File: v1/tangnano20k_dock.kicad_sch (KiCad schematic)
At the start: 50 parts, among them J1 Mini-DIN-6, J2 Conn_01x02, J3 DB15_Female_HighDensity, J4 DB9_Male, J5 Conn_02x16_Odd_Even, J6 FCR684205T, J7 RCA, J8 RCA, J9 RCA, U1 TXS0104E, U2 TangNano20K, U3 CS4354

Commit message: Everything connected
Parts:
- removed J3: DB15_Female_HighDensity, Connector_Dsub:DSUB-15-HD_Female_Horizontal_P2.29x1.98mm_EdgePinOffset9.40mm, symbol Connector:DB15_Female_HighDensity
- removed J5: Conn_02x16_Odd_Even, Connector_PinHeader_2.54mm:PinHeader_2x16_P2.54mm_Vertical, symbol Connector_Generic:Conn_02x16_Odd_Even
- removed J8, J9: RCA, TangNano20k:phono, symbol Connector:Conn_Coaxial
- added J3: DB15_Female_HighDensity_MountingHoles, Connector_Dsub:DSUB-15-HD_Female_Horizontal_P2.29x1.98mm_EdgePinOffset8.35mm_Housed_MountingHolesOffset10.89mm, symbol Connector:DB15_Female_HighDensity_MountingHoles
- added J5, J6: Conn_02x10_Odd_Even, Connector_PinHeader_2.54mm:PinHeader_2x10_P2.54mm_Vertical, symbol Connector_Generic:Conn_02x10_Odd_Even
- added J9: AudioJack3, Connector_Audio:Jack_3.5mm_Lumberg_1503_07_Horizontal, symbol Connector:AudioJack3
- renumbered J6 to J8
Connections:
- net GND: now also J3.0, J3.10, J3.5, J3.6, J3.7, J3.8, J5.1 (Pin_1), J5.2 (Pin_2), J6.1 (Pin_1), J6.2 (Pin_2), J9.S
- net GPIO0: now also J6.3 (Pin_3)
- net GPIO1: now also J6.5 (Pin_5)
- net GPIO10: now also J5.7 (Pin_7)
- net GPIO11: now also J5.9 (Pin_9)
- net GPIO12: now also J5.11 (Pin_11)
- net GPIO13: now also J5.13 (Pin_13)
- net GPIO14: now also J5.15 (Pin_15)
- net GPIO15: now also J5.17 (Pin_17)
- net GPIO2: now also J6.7 (Pin_7)
- net GPIO3: now also J6.9 (Pin_9)
- net GPIO4: now also J6.11 (Pin_11)
- net GPIO5: now also J6.13 (Pin_13)
- net GPIO6: now also J6.15 (Pin_15)
- net GPIO7: now also J6.17 (Pin_17)
- net GPIO8: now also J5.3 (Pin_3)
- net GPIO9: now also J5.5 (Pin_5)
- net VGA_B: now also J3.3
- net VGA_G: now also J3.2
- net VGA_HS: now also J3.13
- net VGA_R: now also J3.1
- net VGA_VS: now also J3.14
- net at RN1.2 (R1): now also J5.4 (Pin_4)
- net at RN1.3 (R2): now also J5.6 (Pin_6)
- net at RN1.4 (R3): now also J5.8 (Pin_8)
- net at RN1.5 (R4): now also J5.10 (Pin_10)
- net at RN1.6 (R5): now also J5.12 (Pin_12)
- net at RN1.7 (R6): now also J5.14 (Pin_14)
- net at RN1.8 (R7): now also J5.16 (Pin_16)
- net at RN1.9 (R8): now also J5.18 (Pin_18)
- net at C10.2, JP2.2 (C): now also J9.T
- net at C11.2, JP3.2 (C): now also J9.R
- net at RN2.2 (R1): now also J6.4 (Pin_4)
- net at RN2.3 (R2): now also J6.6 (Pin_6)
- net at RN2.4 (R3): now also J6.8 (Pin_8)
- net at RN2.5 (R4): now also J6.10 (Pin_10)
- net at RN2.6 (R5): now also J6.12 (Pin_12)
- net at RN2.7 (R6): now also J6.14 (Pin_14)
- net at RN2.8 (R7): now also J6.16 (Pin_16)
- net at RN2.9 (R8): now also J6.18 (Pin_18)
- no-connect marks 8 -> 12
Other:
- note removed: "Left"
- note removed: "Right"
- moved on the sheet: RN1, RN2

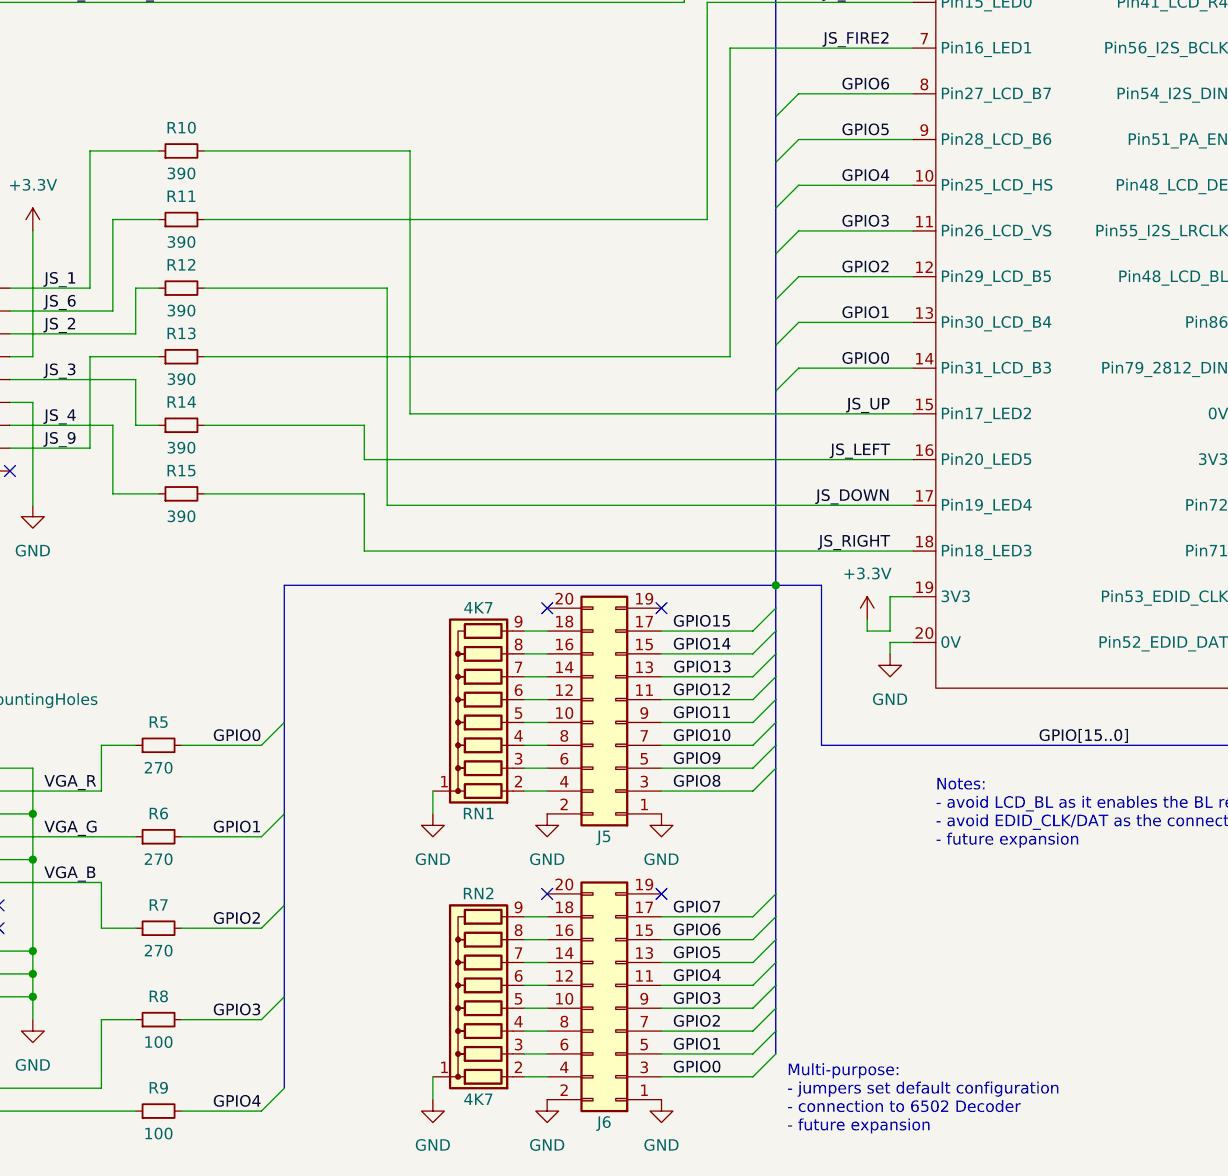
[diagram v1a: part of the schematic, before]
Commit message: Much tidying up, corrected VGA footprint
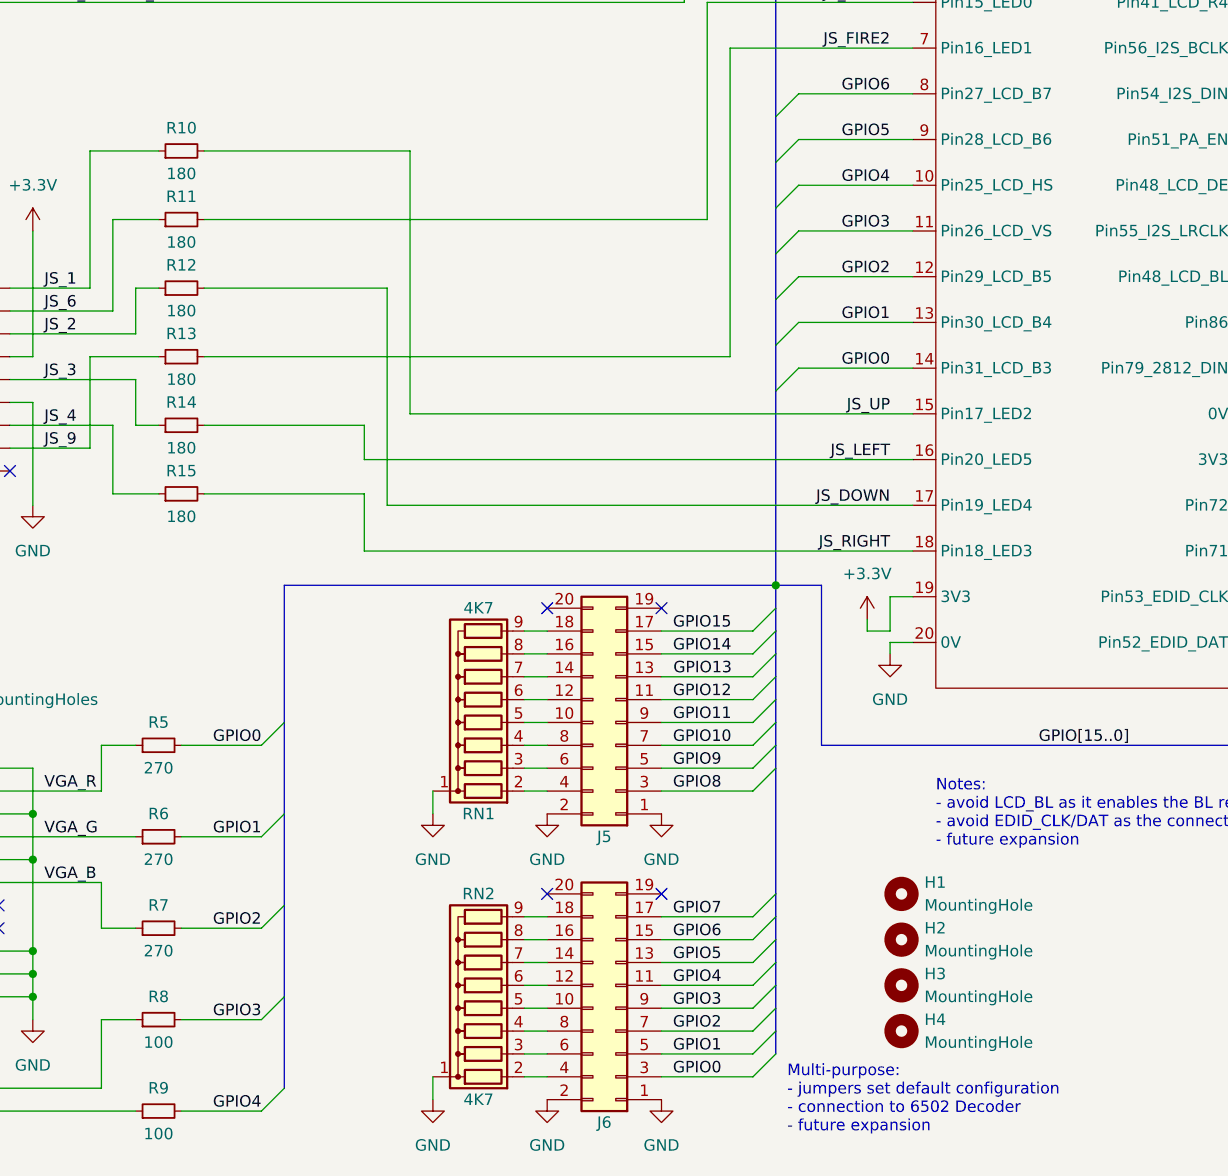
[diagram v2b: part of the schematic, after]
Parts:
- added H1, H2, H3, H4: MountingHole, MountingHole:MountingHole_3.2mm_M3, symbol Mechanical:MountingHole
- J3: footprint Connector_Dsub:DSUB-15-HD_Female_Horizontal_P2.29x1.98mm_EdgePinOffset8.35mm_Housed_MountingHolesOffset10.89mm -> TangNano20k:DSUB-15-HD_Female_Horizontal_P2.29x1.98mm_EdgePinOffset8.35mm_Housed_MountingHolesOffset10.89mm
- J9: footprint Connector_Audio:Jack_3.5mm_Lumberg_1503_07_Horizontal -> TangNano20k:Jack_3.5mm_Lumberg_1503_07_Horizontal
- R10, R11, R12, R13, R14, R15: value 390 -> 180
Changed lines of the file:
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@@
     (property "Reference" "J3" (id 0) (at 33.02 143.51 0))
     (property "Value" "DB15_Female_HighDensity_MountingHoles" (id 1) (at 33.02 146.05 0))
-    (property "Footprint" "Connector_Dsub:DSUB-15-HD_Female_Horizontal_P2.29x1.98mm_EdgePinOffset8.35mm_Housed_MountingHolesOffset10.89mm" (id 2) (at 57.15 156.21 0)
+    (property "Footprint" "TangNano20k:DSUB-15-HD_Female_Horizontal_P2.29x1.98mm_EdgePinOffset8.35mm_Housed_MountingHolesOffset10.89mm" (id 2) (at 57.15 156.21 0)
       (effects (font (size 1.27 1.27)) hide)
     )
@@
     (pin "1")
   )
+  (symbol (lib_id "Mechanical:MountingHole") (at 140.97 182.88 0) (unit 1)
+    (in_bom yes) (on_board yes) (fields_autoplaced)
+    (property "Reference" "H4" (id 0) (at 143.51 181.6099 0)
+      (effects (font (size 1.27 1.27)) (justify left))
+    )
+    (property "Value" "MountingHole" (id 1) (at 143.51 184.1499 0)
+      (effects (font (size 1.27 1.27)) (justify left))
+    )
+    (property "Footprint" "MountingHole:MountingHole_3.2mm_M3" (id 2) (at 140.97 182.88 0)
+      (effects (font (size 1.27 1.27)) hide)
+    )
+    (property "Datasheet" "~" (id 3) (at 140.97 182.88 0)
+      (effects (font (size 1.27 1.27)) hide)
+    )
+  )
   (symbol (lib_id "Device:C_Small") (at 210.82 24.13 0) (mirror x) (unit 1)
     (in_bom yes) (on_board yes) (fields_autoplaced)
@@
     (pin "1")
   )
+  (symbol (lib_id "Mechanical:MountingHole") (at 140.97 167.64 0) (unit 1)
+    (in_bom yes) (on_board yes) (fields_autoplaced)
+    (property "Reference" "H1" (id 0) (at 143.51 166.3699 0)
+      (effects (font (size 1.27 1.27)) (justify left))
+    )
+    (property "Value" "MountingHole" (id 1) (at 143.51 168.9099 0)
+      (effects (font (size 1.27 1.27)) (justify left))
+    )
+    (property "Footprint" "MountingHole:MountingHole_3.2mm_M3" (id 2) (at 140.97 167.64 0)
+      (effects (font (size 1.27 1.27)) hide)
+    )
+    (property "Datasheet" "~" (id 3) (at 140.97 167.64 0)
+      (effects (font (size 1.27 1.27)) hide)
+    )
+  )
   (symbol (lib_id "Device:R_Small") (at 60.96 123.19 90) (unit 1)
     (in_bom yes) (on_board yes)
     (property "Reference" "R15" (id 0) (at 60.96 120.65 90))
-    (property "Value" "390" (id 1) (at 60.96 125.73 90))
+    (property "Value" "180" (id 1) (at 60.96 125.73 90))
     (property "Footprint" "Resistor_THT:R_Axial_DIN0207_L6.3mm_D2.5mm_P10.16mm_Horizontal" (id 2) (at 60.96 123.19 0)
       (effects (font (size 1.27 1.27)) hide)
@@
       (effects (font (size 1.27 1.27)) (justify right))
     )
-    (property "Footprint" "Connector_Audio:Jack_3.5mm_Lumberg_1503_07_Horizontal" (id 2) (at 278.13 109.22 0)
+    (property "Footprint" "TangNano20k:Jack_3.5mm_Lumberg_1503_07_Horizontal" (id 2) (at 278.13 109.22 0)
       (effects (font (size 1.27 1.27)) hide)
     )
@@
     (in_bom yes) (on_board yes)
     (property "Reference" "R11" (id 0) (at 60.96 90.17 90))
-    (property "Value" "390" (id 1) (at 60.96 95.25 90))
+    (property "Value" "180" (id 1) (at 60.96 95.25 90))
     (property "Footprint" "Resistor_THT:R_Axial_DIN0207_L6.3mm_D2.5mm_P10.16mm_Horizontal" (id 2) (at 60.96 92.71 0)
       (effects (font (size 1.27 1.27)) hide)
@@
     (in_bom yes) (on_board yes)
     (property "Reference" "R12" (id 0) (at 60.96 97.79 90))
-    (property "Value" "390" (id 1) (at 60.96 102.87 90))
+    (property "Value" "180" (id 1) (at 60.96 102.87 90))
     (property "Footprint" "Resistor_THT:R_Axial_DIN0207_L6.3mm_D2.5mm_P10.16mm_Horizontal" (id 2) (at 60.96 100.33 0)
       (effects (font (size 1.27 1.27)) hide)
@@
     (pin "8")
     (pin "9")
+  )
+  (symbol (lib_id "Mechanical:MountingHole") (at 140.97 177.8 0) (unit 1)
+    (in_bom yes) (on_board yes) (fields_autoplaced)
+    (property "Reference" "H3" (id 0) (at 143.51 176.5299 0)
+      (effects (font (size 1.27 1.27)) (justify left))
+    )
+    (property "Value" "MountingHole" (id 1) (at 143.51 179.0699 0)
+      (effects (font (size 1.27 1.27)) (justify left))
+    )
+    (property "Footprint" "MountingHole:MountingHole_3.2mm_M3" (id 2) (at 140.97 177.8 0)
+      (effects (font (size 1.27 1.27)) hide)
+    )
+    (property "Datasheet" "~" (id 3) (at 140.97 177.8 0)
+      (effects (font (size 1.27 1.27)) hide)
+    )
   )
   (symbol (lib_id "Device:R_Small") (at 58.42 151.13 90) (unit 1)
@@
     (in_bom yes) (on_board yes)
     (property "Reference" "R13" (id 0) (at 60.96 105.41 90))
-    (property "Value" "390" (id 1) (at 60.96 110.49 90))
+    (property "Value" "180" (id 1) (at 60.96 110.49 90))
     (property "Footprint" "Resistor_THT:R_Axial_DIN0207_L6.3mm_D2.5mm_P10.16mm_Horizontal" (id 2) (at 60.96 107.95 0)
       (effects (font (size 1.27 1.27)) hide)
@@
     (in_bom yes) (on_board yes)
     (property "Reference" "R14" (id 0) (at 60.96 113.03 90))
-    (property "Value" "390" (id 1) (at 60.96 118.11 90))
+    (property "Value" "180" (id 1) (at 60.96 118.11 90))
     (property "Footprint" "Resistor_THT:R_Axial_DIN0207_L6.3mm_D2.5mm_P10.16mm_Horizontal" (id 2) (at 60.96 115.57 0)
       (effects (font (size 1.27 1.27)) hide)
@@
     (in_bom yes) (on_board yes)
     (property "Reference" "R10" (id 0) (at 60.96 82.55 90))
-    (property "Value" "390" (id 1) (at 60.96 87.63 90))
+    (property "Value" "180" (id 1) (at 60.96 87.63 90))
     (property "Footprint" "Resistor_THT:R_Axial_DIN0207_L6.3mm_D2.5mm_P10.16mm_Horizontal" (id 2) (at 60.96 85.09 0)
       (effects (font (size 1.27 1.27)) hide)
@@
     (pin "1")
   )
+  (symbol (lib_id "Mechanical:MountingHole") (at 140.97 172.72 0) (unit 1)
+    (in_bom yes) (on_board yes) (fields_autoplaced)
+    (property "Reference" "H2" (id 0) (at 143.51 171.4499 0)
+      (effects (font (size 1.27 1.27)) (justify left))
+    )
+    (property "Value" "MountingHole" (id 1) (at 143.51 173.9899 0)
+      (effects (font (size 1.27 1.27)) (justify left))
+    )
+    (property "Footprint" "MountingHole:MountingHole_3.2mm_M3" (id 2) (at 140.97 172.72 0)
+      (effects (font (size 1.27 1.27)) hide)
+    )
+    (property "Datasheet" "~" (id 3) (at 140.97 172.72 0)
+      (effects (font (size 1.27 1.27)) hide)
+    )
+  )
   (symbol (lib_id "power:GND") (at 245.11 38.1 0) (unit 1)
     (in_bom yes) (on_board yes) (fields_autoplaced)
@@
       (reference "C11") (unit 1) (value "2n2") (footprint "Capacitor_THT:C_Disc_D5.0mm_W2.5mm_P2.50mm")
     )
+    (path "/3efa4c66-1bea-40a4-bda9-02b28c07af29"
+      (reference "H1") (unit 1) (value "MountingHole") (footprint "MountingHole:MountingHole_3.2mm_M3")
+    )
+    (path "/f95e5f0b-56a0-442b-9f1b-cce491951b72"
+      (reference "H2") (unit 1) (value "MountingHole") (footprint "MountingHole:MountingHole_3.2mm_M3")
+    )
+    (path "/820967dd-e818-4da1-bb9b-2a6bbdeea89d"
+      (reference "H3") (unit 1) (value "MountingHole") (footprint "MountingHole:MountingHole_3.2mm_M3")
+    )
+    (path "/2edda0e4-403b-45ec-b8d6-bae5fe9a549d"
+      (reference "H4") (unit 1) (value "MountingHole") (footprint "MountingHole:MountingHole_3.2mm_M3")
+    )
     (path "/9becf180-126c-4cc1-ba0f-3c658ab540d4"
       (reference "J1") (unit 1) (value "Mini-DIN-6") (footprint "TangNano20k:minidin6")
@@
     )
     (path "/06f8946b-c0d3-4d8e-bc44-a3a97fa77958"
-      (reference "J3") (unit 1) (value "DB15_Female_HighDensity_MountingHoles") (footprint "Connector_Dsub:DSUB-15-HD_Female_Horizontal_P2.29x1.98mm_EdgePinOffset8.35mm_Housed_MountingHolesOffset10.89mm")
+      (reference "J3") (unit 1) (value "DB15_Female_HighDensity_MountingHoles") (footprint "TangNano20k:DSUB-15-HD_Female_Horizontal_P2.29x1.98mm_EdgePinOffset8.35mm_Housed_MountingHolesOffset10.89mm")
     )
     (path "/8d13ec8a-0e85-4cb6-815a-22cecb20a93c"
@@
     )
     (path "/4877468b-ee74-43f7-a4dc-6a0ddb9f2b4d"
-      (reference "J9") (unit 1) (value "AudioJack3") (footprint "Connector_Audio:Jack_3.5mm_Lumberg_1503_07_Horizontal")
+      (reference "J9") (unit 1) (value "AudioJack3") (footprint "TangNano20k:Jack_3.5mm_Lumberg_1503_07_Horizontal")
     )
     (path "/af9d2222-45eb-4253-a2c0-2a0bf1e346a6"
@@
     )
     (path "/ec860be2-adfe-4b02-922f-502025aff678"
-      (reference "R10") (unit 1) (value "390") (footprint "Resistor_THT:R_Axial_DIN0207_L6.3mm_D2.5mm_P10.16mm_Horizontal")
+      (reference "R10") (unit 1) (value "180") (footprint "Resistor_THT:R_Axial_DIN0207_L6.3mm_D2.5mm_P10.16mm_Horizontal")
     )
     (path "/4daadee8-7130-4109-85dc-93cbc1883675"
-      (reference "R11") (unit 1) (value "390") (footprint "Resistor_THT:R_Axial_DIN0207_L6.3mm_D2.5mm_P10.16mm_Horizontal")
+      (reference "R11") (unit 1) (value "180") (footprint "Resistor_THT:R_Axial_DIN0207_L6.3mm_D2.5mm_P10.16mm_Horizontal")
     )
     (path "/68db8968-573a-47f1-98e2-101734857163"
-      (reference "R12") (unit 1) (value "390") (footprint "Resistor_THT:R_Axial_DIN0207_L6.3mm_D2.5mm_P10.16mm_Horizontal")
+      (reference "R12") (unit 1) (value "180") (footprint "Resistor_THT:R_Axial_DIN0207_L6.3mm_D2.5mm_P10.16mm_Horizontal")
     )
     (path "/956cf817-2d1c-478e-a791-f49eab8e02c8"
-      (reference "R13") (unit 1) (value "390") (footprint "Resistor_THT:R_Axial_DIN0207_L6.3mm_D2.5mm_P10.16mm_Horizontal")
+      (reference "R13") (unit 1) (value "180") (footprint "Resistor_THT:R_Axial_DIN0207_L6.3mm_D2.5mm_P10.16mm_Horizontal")
     )
     (path "/a38abefa-0023-495c-991e-ff626bbcf6e2"
-      (reference "R14") (unit 1) (value "390") (footprint "Resistor_THT:R_Axial_DIN0207_L6.3mm_D2.5mm_P10.16mm_Horizontal")
+      (reference "R14") (unit 1) (value "180") (footprint "Resistor_THT:R_Axial_DIN0207_L6.3mm_D2.5mm_P10.16mm_Horizontal")
     )
     (path "/416107c6-4f9e-43f1-b98e-04e1c0393574"
-      (reference "R15") (unit 1) (value "390") (footprint "Resistor_THT:R_Axial_DIN0207_L6.3mm_D2.5mm_P10.16mm_Horizontal")
+      (reference "R15") (unit 1) (value "180") (footprint "Resistor_THT:R_Axial_DIN0207_L6.3mm_D2.5mm_P10.16mm_Horizontal")
     )
     (path "/02e005ab-d466-403f-a516-098fae9061ff"
